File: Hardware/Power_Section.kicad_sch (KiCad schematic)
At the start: 39 parts, among them IC1 TPS54202HDDCR, Q1 SI2347DS-T1-GE3, U1 TLV743P, U2 TLV743P, U3 TLV743P, U4 TLV743P

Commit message: Changes in CAN section
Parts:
- removed D6: 3.6V/400W, Package_TO_SOT_SMD:SOT-23-6, symbol Power_Protection:ESDA5V3SC5
- removed D7: 5.3V/400W, Package_TO_SOT_SMD:SOT-23-3, symbol Power_Protection:ESDA5V3L
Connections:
- no-connect marks 1 -> 0

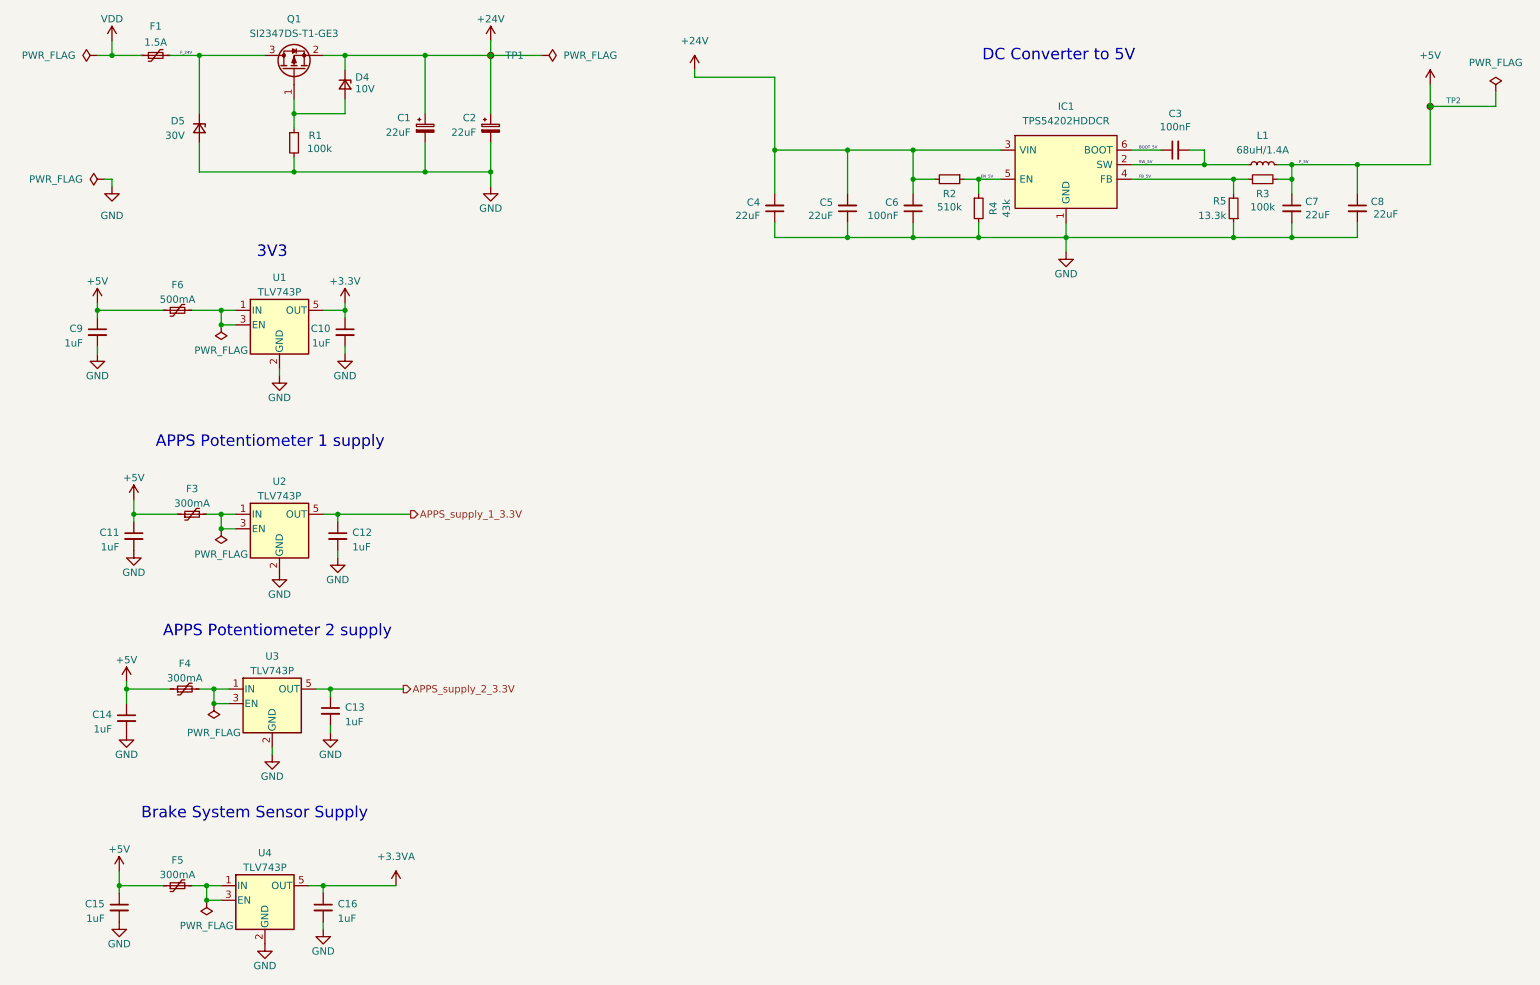
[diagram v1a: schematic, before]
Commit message: Changes in schematic, separated CAN buses, added XIAO Sense S3 DevBoard
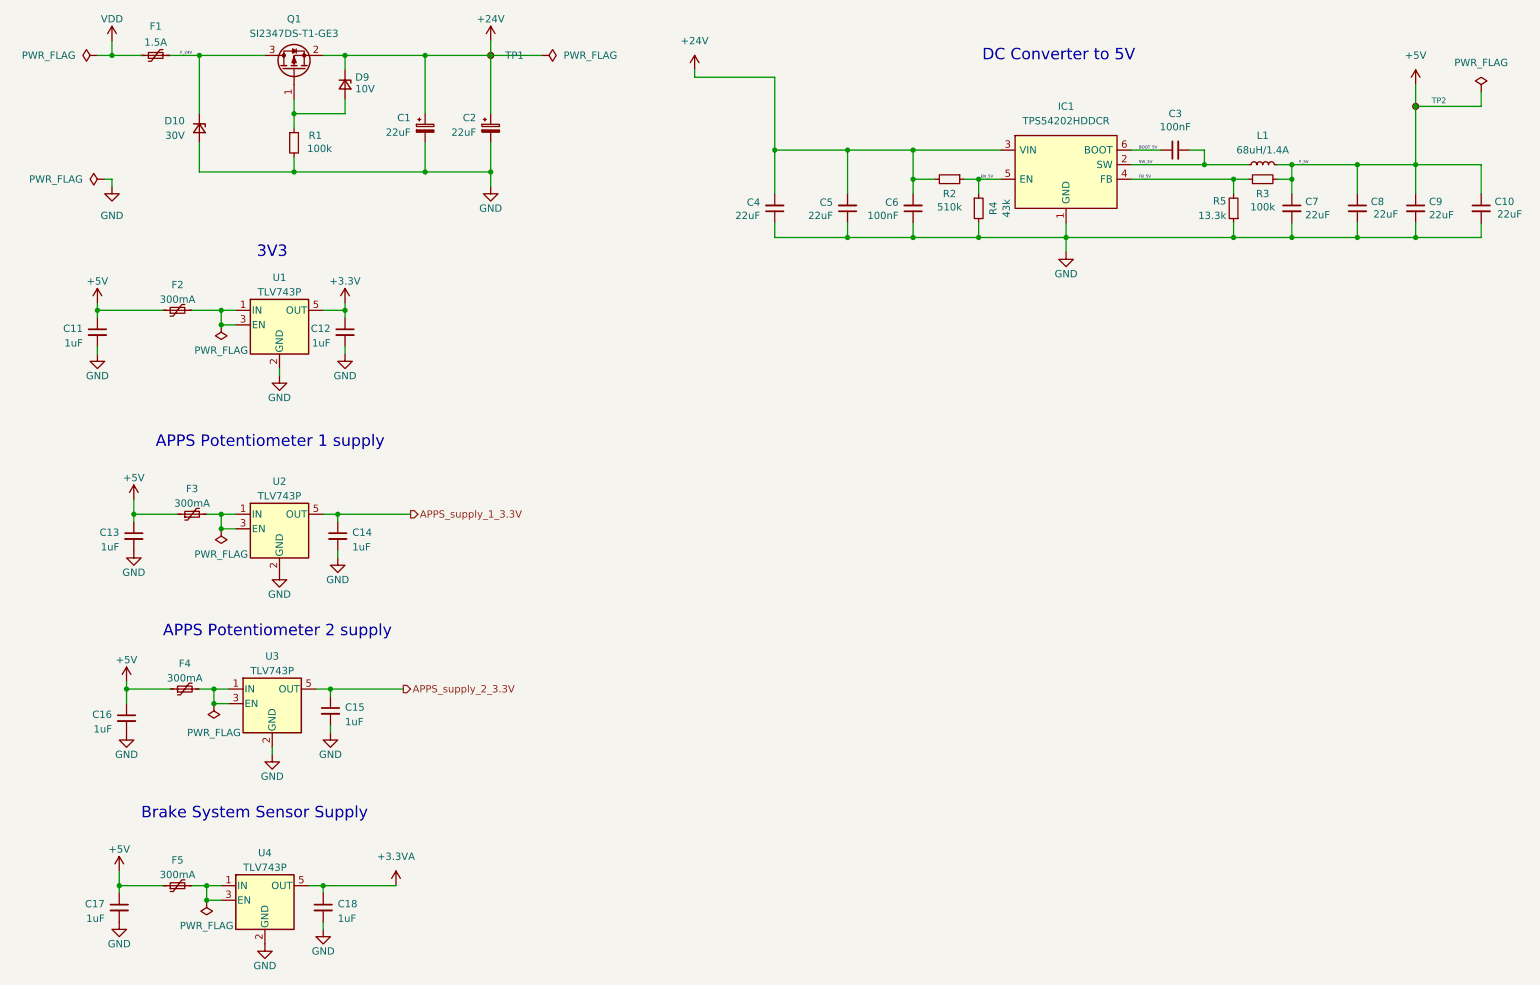
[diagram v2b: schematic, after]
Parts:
- added C10, C9: 22uF, Capacitor_SMD:C_0805_2012Metric, symbol Device:C_Small
- F2: renamed from F6; value 500mA -> 300mA
- renumbered C9 to C11, C10 to C12, C11 to C13, C12 to C14, C13 to C15, C14 to C16, C15 to C17, C16 to C18, D5 to D10, D4 to D9
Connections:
- net +5V: now also C10.1, C9.1
- net GND: now also C10.2, C9.2
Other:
- moved on the sheet: TP2

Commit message: Changes in CAN section
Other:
- title: (none) -> FrontBox
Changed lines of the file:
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@@
 	(generator_version "9.0")
 	(paper "A4")
+	(title_block
+		(title "FrontBox")
+	)
 	(text "APPS Potentiometer 2 supply"
 		(exclude_from_sim no)
@@
 	)
 	(junction
-		(at 64.77 172.72)
-		(diameter 0)
-		(color 0 0 0 0)
-	)
-	(junction
 		(at 245.11 59.69)
 		(diameter 0)
@@
 	)
 	(junction
+		(at 64.77 172.72)
+		(diameter 0)
+		(color 0 0 0 0)
+	)
+	(junction
 		(at 218.44 46.99)
 		(diameter 0)
@@
 	(wire
 		(pts
-			(xy 64.77 172.72) (xy 77.47 172.72)
-		)
-		(stroke
-			(width 0)
-			(type default)
-		)
-	)
-	(wire
-		(pts
 			(xy 25.4 72.39) (xy 25.4 73.66)
 		)
@@
 	(wire
 		(pts
+			(xy 64.77 172.72) (xy 78.74 172.72)
+		)
+		(stroke
+			(width 0)
+			(type default)
+		)
+	)
+	(wire
+		(pts
 			(xy 25.4 78.74) (xy 25.4 80.01)
 		)
@@
 	(wire
 		(pts
+			(xy 78.74 172.72) (xy 78.74 170.18)
+		)
+		(stroke
+			(width 0)
+			(type default)
+		)
+	)
+	(wire
+		(pts
 			(xy 245.11 46.99) (xy 255.27 46.99)
 		)
@@
 	(symbol
 		(lib_id "power:+3.3VA")
-		(at 77.47 172.72 0)
+		(at 78.74 170.18 0)
 		(unit 1)
 		(exclude_from_sim no)
@@
 		(dnp no)
 		(property "Reference" "#PWR036"
-			(at 77.47 176.53 0)
+			(at 78.74 173.99 0)
 			(effects
 				(font
@@
 		)
 		(property "Value" "+3.3VA"
-			(at 77.47 167.64 0)
+			(at 78.74 165.1 0)
 			(effects
 				(font
@@
 		)
 		(property "Footprint" ""
-			(at 77.47 172.72 0)
+			(at 78.74 170.18 0)
 			(effects
 				(font
@@
 		)
 		(property "Datasheet" ""
-			(at 77.47 172.72 0)
+			(at 78.74 170.18 0)
 			(effects
 				(font
@@
 		)
 		(property "Description" ""
-			(at 77.47 172.72 0)
+			(at 78.74 170.18 0)
 			(effects
 				(font

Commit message: BOM update
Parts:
- C11, C12, C13, C14, C15, C16, C17, C18, R1: Mouser Part Number (none) -> .
- F1: Mouser Part Number (none) -> 504-PTS181233V075
- F2, F3, F4, F5: Mouser Part Number (none) -> 603-SMD0603B010TF
- Q1: Mouser Part Number (none) -> 78-SI2347DS-T1-GE3
- U1, U2, U3, U4: Mouser Part Number (none) -> 595-TLV74333PDBVR
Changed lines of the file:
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@@
 			)
 		)
+		(property "Mouser Part Number" "."
+			(at 31.75 111.76 0)
+			(effects
+				(font
+					(size 1.27 1.27)
+				)
+			)
+		)
 		(pin "1"
 		)
@@
 			)
 		)
+		(property "Mouser Part Number" "78-SI2347DS-T1-GE3"
+			(at 59.69 30.48 0)
+			(effects
+				(font
+					(size 1.27 1.27)
+				)
+				(hide yes)
+			)
+		)
 		(pin "2"
 		)
@@
 			)
 		)
+		(property "Mouser Part Number" "504-PTS181233V075"
+			(at 35.56 27.94 0)
+			(effects
+				(font
+					(size 1.27 1.27)
+				)
+				(hide yes)
+			)
+		)
 		(pin "1"
 		)
@@
 			)
 		)
+		(property "Mouser Part Number" "."
+			(at 25.4 76.2 0)
+			(effects
+				(font
+					(size 1.27 1.27)
+				)
+			)
+		)
 		(pin "1"
 		)
@@
 			)
 		)
+		(property "Mouser Part Number" "603-SMD0603B010TF"
+			(at 39.37 172.72 0)
+			(effects
+				(font
+					(size 1.27 1.27)
+				)
+				(hide yes)
+			)
+		)
 		(pin "1"
 		)
@@
 			)
 		)
+		(property "Mouser Part Number" "603-SMD0603B010TF"
+			(at 40.64 138.43 0)
+			(effects
+				(font
+					(size 1.27 1.27)
+				)
+				(hide yes)
+			)
+		)
 		(pin "1"
 		)
@@
 			)
 		)
+		(property "Mouser Part Number" "."
+			(at 30.48 143.51 0)
+			(effects
+				(font
+					(size 1.27 1.27)
+				)
+			)
+		)
 		(pin "1"
 		)
@@
 			)
 		)
+		(property "Mouser Part Number" "595-TLV74333PDBVR"
+			(at 57.15 110.49 0)
+			(effects
+				(font
+					(size 1.27 1.27)
+				)
+				(hide yes)
+			)
+		)
 		(pin "1"
 		)
@@
 			)
 		)
+		(property "Mouser Part Number" "595-TLV74333PDBVR"
+			(at 57.15 74.93 0)
+			(effects
+				(font
+					(size 1.27 1.27)
+				)
+				(hide yes)
+			)
+		)
 		(pin "1"
 		)
@@
 			)
 		)
+		(property "Mouser Part Number" "."
+			(at 68.58 76.2 0)
+			(effects
+				(font
+					(size 1.27 1.27)
+				)
+			)
+		)
 		(pin "1"
 		)
@@
 			)
 		)
+		(property "Mouser Part Number" "."
+			(at 59.69 43.18 0)
+			(effects
+				(font
+					(size 1.27 1.27)
+				)
+			)
+		)
 		(pin "2"
 		)
@@
 			)
 		)
+		(property "Mouser Part Number" "."
+			(at 29.21 176.53 0)
+			(effects
+				(font
+					(size 1.27 1.27)
+				)
+			)
+		)
 		(pin "1"
 		)
@@
 			)
 		)
+		(property "Mouser Part Number" "595-TLV74333PDBVR"
+			(at 55.88 140.97 0)
+			(effects
+				(font
+					(size 1.27 1.27)
+				)
+				(hide yes)
+			)
+		)
 		(pin "1"
 		)
@@
 			)
 		)
+		(property "Mouser Part Number" "603-SMD0603B010TF"
+			(at 39.37 72.39 0)
+			(effects
+				(font
+					(size 1.27 1.27)
+				)
+				(hide yes)
+			)
+		)
 		(pin "1"
 		)
@@
 			)
 		)
+		(property "Mouser Part Number" "."
+			(at 64.77 176.53 0)
+			(effects
+				(font
+					(size 1.27 1.27)
+				)
+			)
+		)
 		(pin "1"
 		)
@@
 			)
 		)
+		(property "Mouser Part Number" "."
+			(at 66.04 142.24 0)
+			(effects
+				(font
+					(size 1.27 1.27)
+				)
+			)
+		)
 		(pin "1"
 		)
@@
 			)
 		)
+		(property "Mouser Part Number" "603-SMD0603B010TF"
+			(at 41.91 107.95 0)
+			(effects
+				(font
+					(size 1.27 1.27)
+				)
+				(hide yes)
+			)
+		)
 		(pin "1"
 		)
@@
 			)
 		)
+		(property "Mouser Part Number" "."
+			(at 67.31 111.76 0)
+			(effects
+				(font
+					(size 1.27 1.27)
+				)
+			)
+		)
 		(pin "1"
 		)
@@
 			(at 54.61 175.26 0)
 			(effects
+				(font
+					(size 1.27 1.27)
+				)
+				(hide yes)
+			)
+		)
+		(property "Mouser Part Number" "595-TLV74333PDBVR"
+			(at 54.61 175.26 0)
+			(effects
